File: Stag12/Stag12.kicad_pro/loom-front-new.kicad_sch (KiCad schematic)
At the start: 10 parts

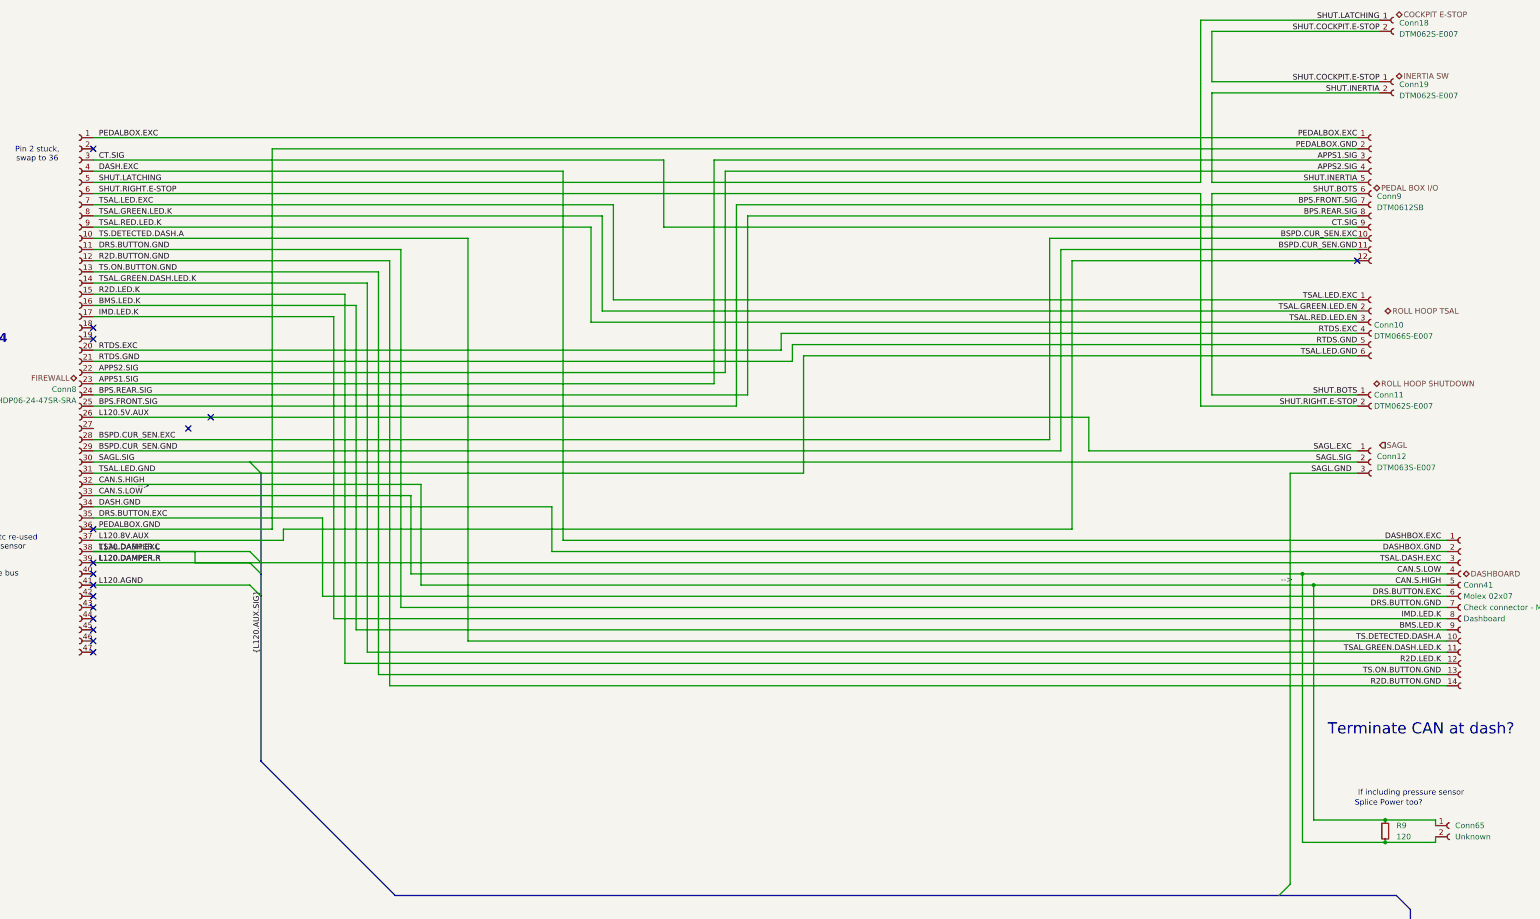
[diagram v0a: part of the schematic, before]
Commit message: Started new Front Box loom
now with buses!
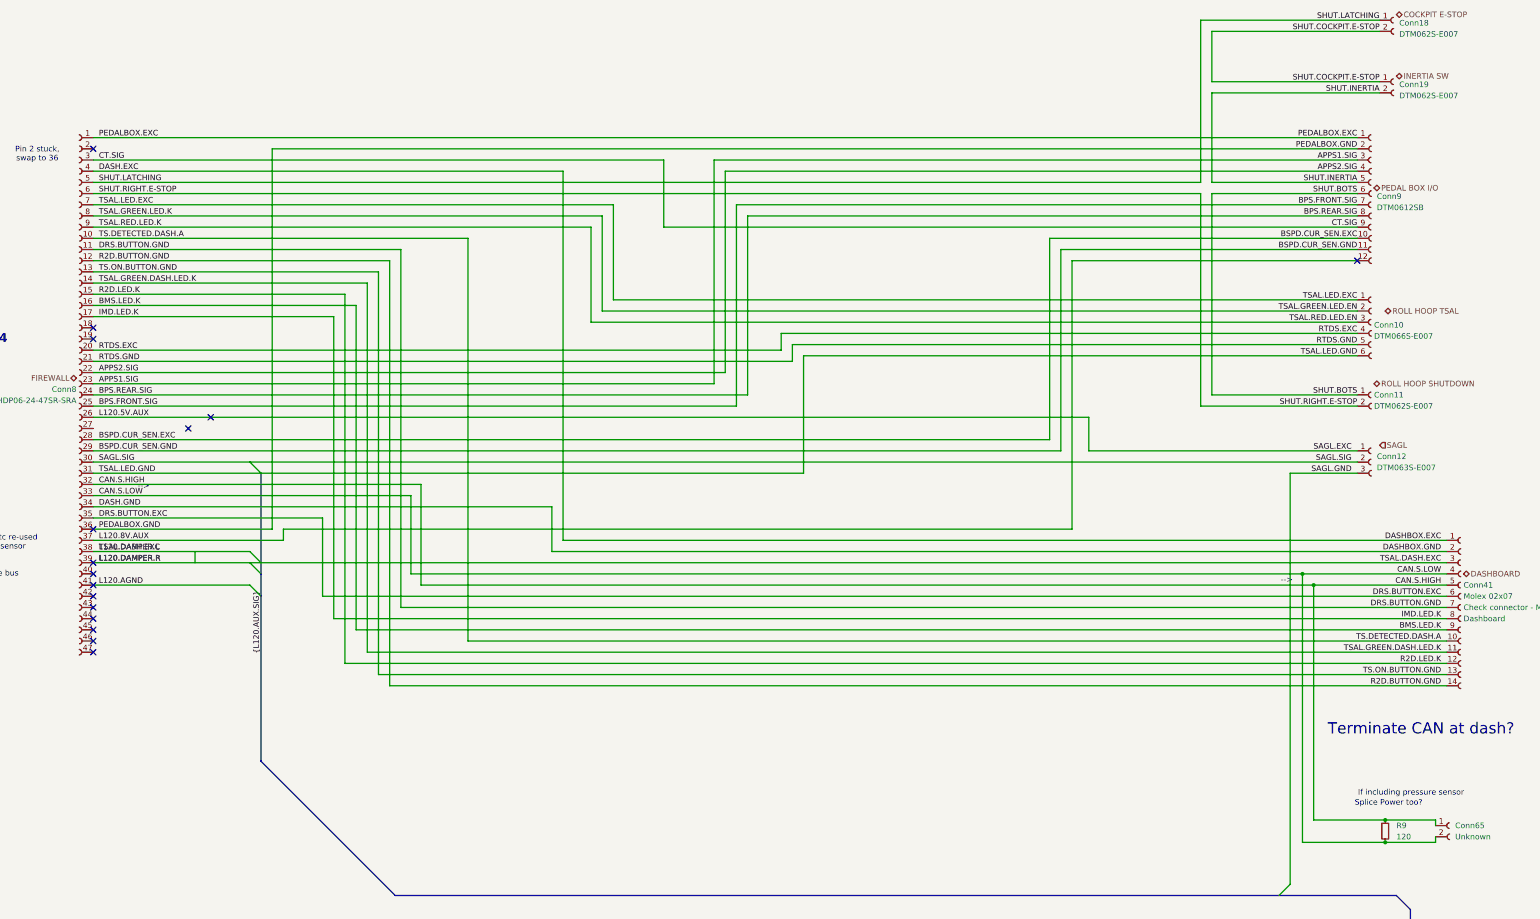
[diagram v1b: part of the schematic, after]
